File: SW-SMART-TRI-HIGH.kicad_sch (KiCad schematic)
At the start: 53 parts, among them J1 SWLINK, J2 USART1, J3 POWER_OUT, SW0 BTS7002-1EPP, SW1 BTS7002-1EPP, SW2 BTS7002-1EPP, U1 STM32G0B1KBTx, U4 MCP2562-E-SN

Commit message: renamed power in connector
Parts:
- J3: value POWER_OUT -> POWER OUT
- J4: renamed from POWER_IN1; value PWRIN -> POWER IN
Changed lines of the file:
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@@
 		(dnp no)
 		(fields_autoplaced yes)
-		(property "Reference" "POWER_IN1"
+		(property "Reference" "J4"
 			(at 80.01 39.37 0)
 			(effects
@@
 			)
 		)
-		(property "Value" "PWRIN"
+		(property "Value" "POWER IN"
 			(at 80.01 41.91 0)
 			(effects
@@
 					(size 1.27 1.27)
 				)
-				(hide yes)
 			)
 		)
@@
 			(project "SW-DUAL-10A"
 				(path "/08d9f551-d314-4c5c-859f-da02a807087d"
-					(reference "POWER_IN1")
+					(reference "J4")
 					(unit 1)
 				)
@@
 			)
 		)
-		(property "Value" "POWER_OUT"
+		(property "Value" "POWER OUT"
 			(at 149.86 148.5901 0)
 			(effects

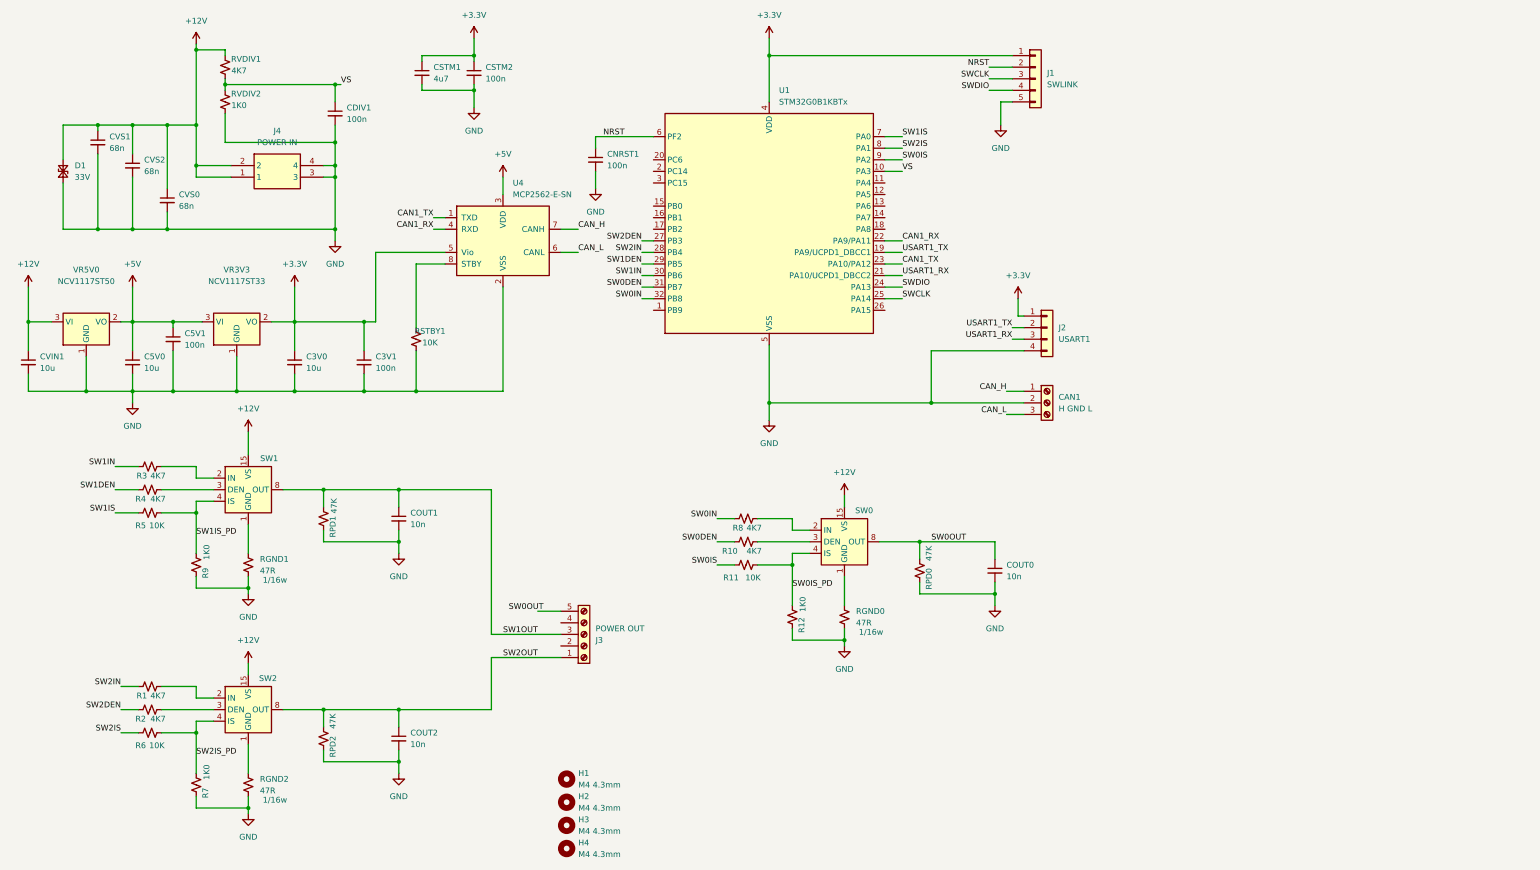
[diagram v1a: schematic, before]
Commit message: switch to smps for 5v, adjust CAN and SWD pin connections
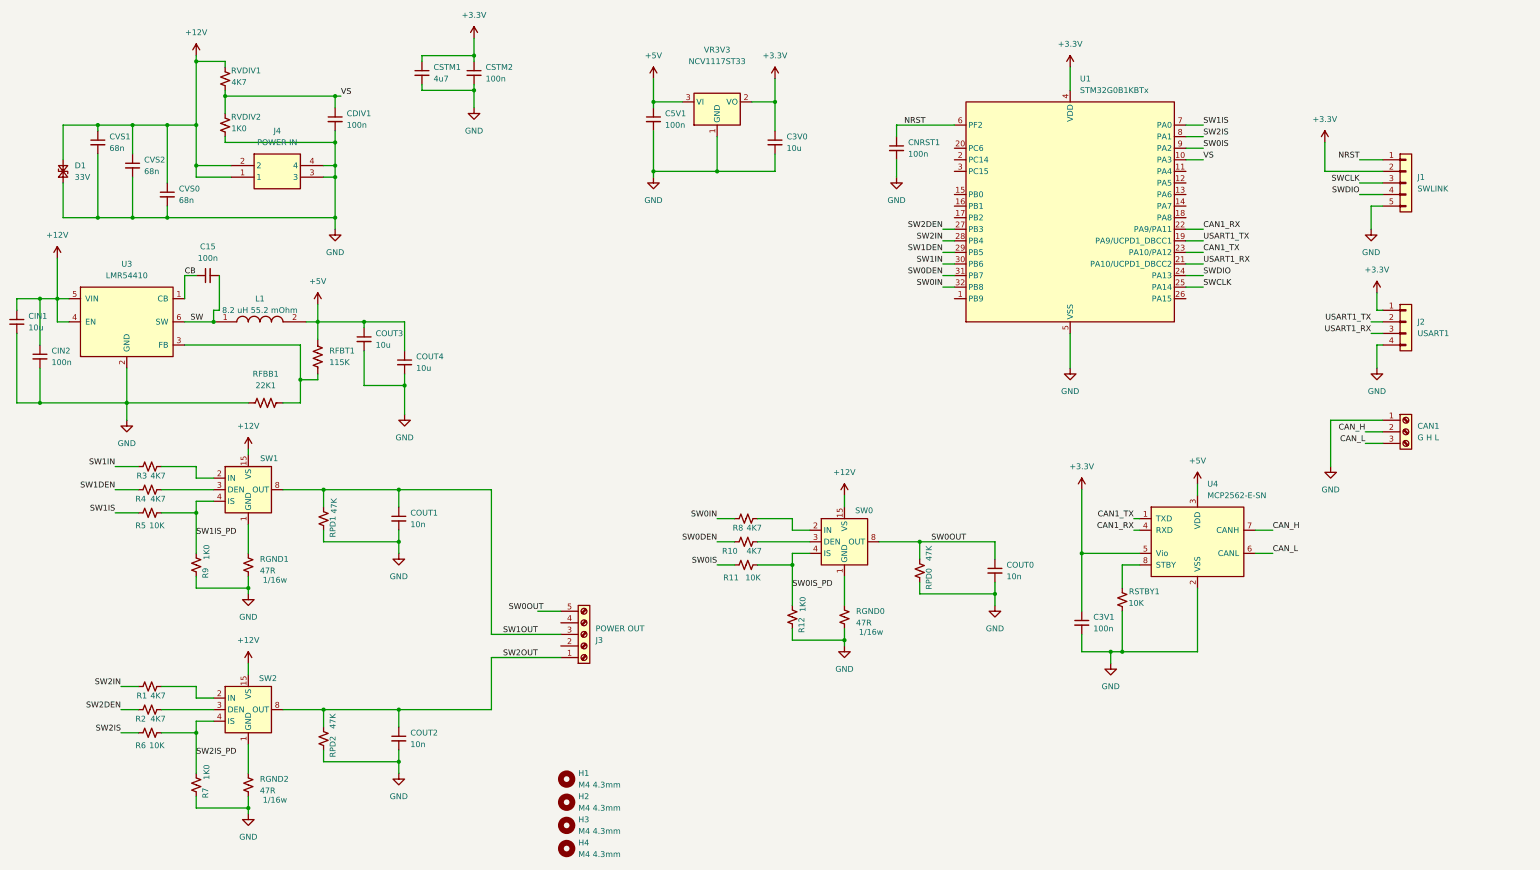
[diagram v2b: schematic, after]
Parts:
- removed C5V0: 10u, Capacitor_SMD:C_0805_2012Metric_Pad1.18x1.45mm_HandSolder, symbol Device:C_Small
- removed CVIN1: 10u, Capacitor_SMD:C_1206_3216Metric_Pad1.33x1.80mm_HandSolder, symbol Device:C_Small
- removed VR5V0: NCV1117ST50, PCM_SparkFun-Semiconductor-Standard:SOT-223-3_TabPin2, symbol PCM_SparkFun-Regulator:LM1117-3.3
- added C15, CIN2: 100n, Capacitor_SMD:C_0603_1608Metric_Pad1.08x0.95mm_HandSolder, symbol Device:C_Small
- added CIN1: 10u, Capacitor_SMD:C_1210_3225Metric_Pad1.33x2.70mm_HandSolder, symbol Device:C_Small
- added COUT3, COUT4: 10u, Capacitor_SMD:C_0805_2012Metric_Pad1.18x1.45mm_HandSolder, symbol Device:C_Small
- added L1: 8.2 uH 55.2 mOhm, SRP5030HMT2R2M, symbol SamacSys_Parts:SRP5030HMT-8R2M
- added RFBB1: 22K1, Resistor_SMD:R_0603_1608Metric_Pad0.98x0.95mm_HandSolder, symbol Device:R_US
- added RFBT1: 115K, Resistor_SMD:R_0603_1608Metric_Pad0.98x0.95mm_HandSolder, symbol Device:R_US
- added U3: LMR54410, Package_TO_SOT_SMD:SOT-23-6, symbol Regulator_Switching:LMR50410
- CAN1: value H GND L -> G H L; footprint TerminalBlock_Phoenix:TerminalBlock_Phoenix_MKDS-1,5-3-5.08_1x03_P5.08mm_Horizontal -> TerminalBlock_Phoenix:TerminalBlock_Phoenix_MPT-0,5-3-2.54_1x03_P2.54mm_Horizontal
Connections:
- net +12V: now also CIN1.1, CIN2.1, U3.4 (EN), U3.5 (VIN)
- net +3.3V: now also J1.2 (Pin_2); no longer J1.1 (Pin_1)
- net +5V: now also COUT3.1, COUT4.1, L1.2, RFBT1.1
- net CAN_H: now also CAN1.2 (Pin_2); no longer CAN1.1 (Pin_1)
- net GND: now also CAN1.1 (Pin_1), CIN1.2, CIN2.2, COUT3.2, COUT4.2, RFBB1.1, U3.2 (GND); no longer CAN1.2 (Pin_2)
- net NRST: now also J1.1 (Pin_1); no longer J1.2 (Pin_2)
- new net: RFBB1.2, RFBT1.2, U3.3 (FB)
- new net CB: C15.1, U3.1 (CB)
- new net SW: C15.2, L1.1, U3.6 (SW)
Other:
- moved on the sheet: C3V0, C3V1, C5V1, CAN1, CDIV1, CNRST1, CVS0, J1, J2, RSTBY1, RVDIV1, RVDIV2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

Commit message: improve ground connections, cleanup silkscreen
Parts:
- SW0: footprint SamacSys_Parts:SOP65P600X115-15N -> Package_SO:Infineon_PG-TSDSO-14-22
- SWD1: renamed from J1; value SWLINK -> RST 3V3 CLK DIO GND; footprint PCM_SparkFun-Connector:1x05_P2.54mm_Locking -> Connector_PinHeader_2.54mm:PinHeader_1x05_P2.54mm_Vertical
- USART1: renamed from J2; value USART1 -> 3V3 TX RX GND; footprint PCM_SparkFun-Connector:1x04_P2.54mm_Locking -> Connector_PinHeader_2.54mm:PinHeader_1x04_P2.54mm_Vertical
- renumbered C15 to CB1
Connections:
- net FB: now reaches RFBB1.2, RFBT1.2, U3.3 (FB)
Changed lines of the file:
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@@
 		)
 	)
+	(label "FB"
+		(at 67.31 86.36 0)
+		(effects
+			(font
+				(size 1.27 1.27)
+			)
+			(justify left bottom)
+		)
+	)
 	(label "SW2DEN"
 		(at 45.72 166.37 180)
@@
 			)
 		)
-		(property "Footprint" "SamacSys_Parts:SOP65P600X115-15N"
+		(property "Footprint" "Package_SO:Infineon_PG-TSDSO-14-22"
 			(at 181.61 135.89 0)
 			(effects
@@
 		(dnp no)
 		(fields_autoplaced yes)
-		(property "Reference" "C15"
+		(property "Reference" "CB1"
 			(at 64.7763 64.77 90)
 			(effects
@@
 			(project "SW-SMART-TRI-HIGH"
 				(path "/08d9f551-d314-4c5c-859f-da02a807087d"
-					(reference "C15")
+					(reference "CB1")
 					(unit 1)
 				)
@@
 		(dnp no)
 		(fields_autoplaced yes)
-		(property "Reference" "J1"
+		(property "Reference" "SWD1"
 			(at 330.2 49.5299 0)
 			(effects
@@
 			)
 		)
-		(property "Value" "SWLINK"
+		(property "Value" "RST 3V3 CLK DIO GND"
 			(at 330.2 52.0699 0)
 			(effects
@@
 			)
 		)
-		(property "Footprint" "PCM_SparkFun-Connector:1x05_P2.54mm_Locking"
+		(property "Footprint" "Connector_PinHeader_2.54mm:PinHeader_1x05_P2.54mm_Vertical"
 			(at 327.66 50.8 0)
 			(effects
@@
 			(project ""
 				(path "/08d9f551-d314-4c5c-859f-da02a807087d"
-					(reference "J1")
+					(reference "SWD1")
 					(unit 1)
 				)
@@
 		(dnp no)
 		(fields_autoplaced yes)
-		(property "Reference" "J2"
+		(property "Reference" "USART1"
 			(at 330.2 81.2799 0)
 			(effects
@@
 			)
 		)
-		(property "Value" "USART1"
+		(property "Value" "3V3 TX RX GND"
 			(at 330.2 83.8199 0)
 			(effects
@@
 			)
 		)
-		(property "Footprint" "PCM_SparkFun-Connector:1x04_P2.54mm_Locking"
+		(property "Footprint" "Connector_PinHeader_2.54mm:PinHeader_1x04_P2.54mm_Vertical"
 			(at 327.66 81.28 0)
 			(effects
@@
 			(project ""
 				(path "/08d9f551-d314-4c5c-859f-da02a807087d"
-					(reference "J2")
+					(reference "USART1")
 					(unit 1)
 				)

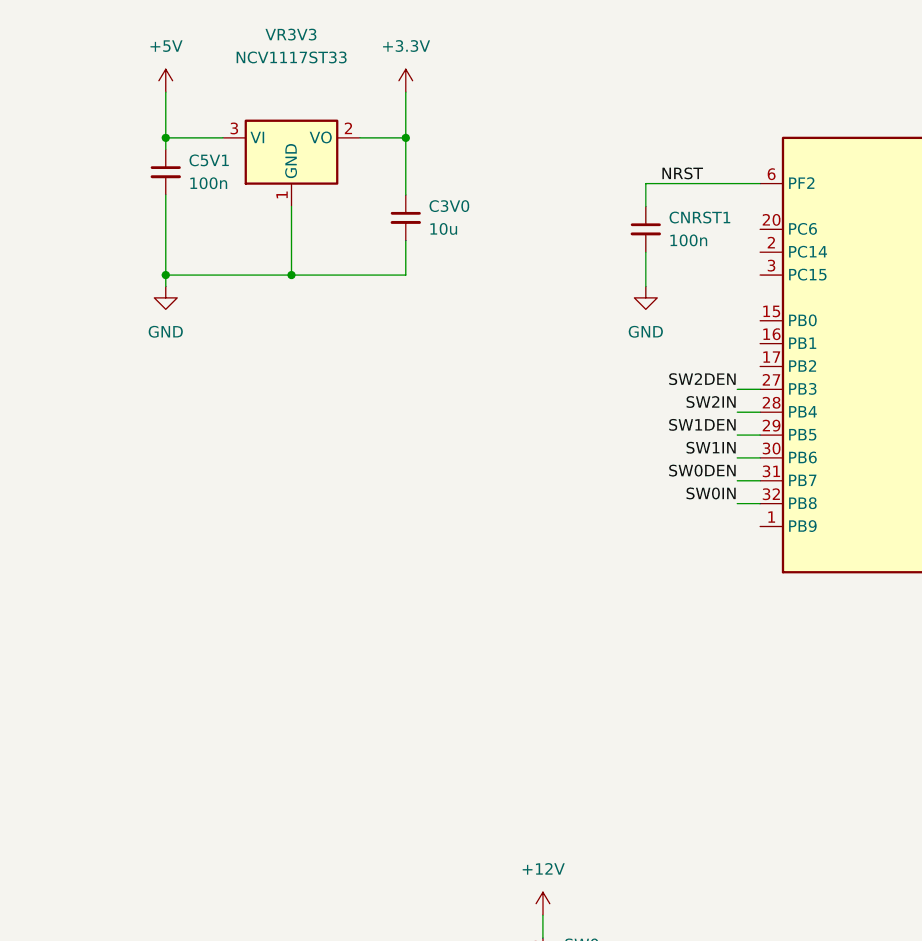
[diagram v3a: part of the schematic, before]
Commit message: add 8mhz XO, fix some footprint issues
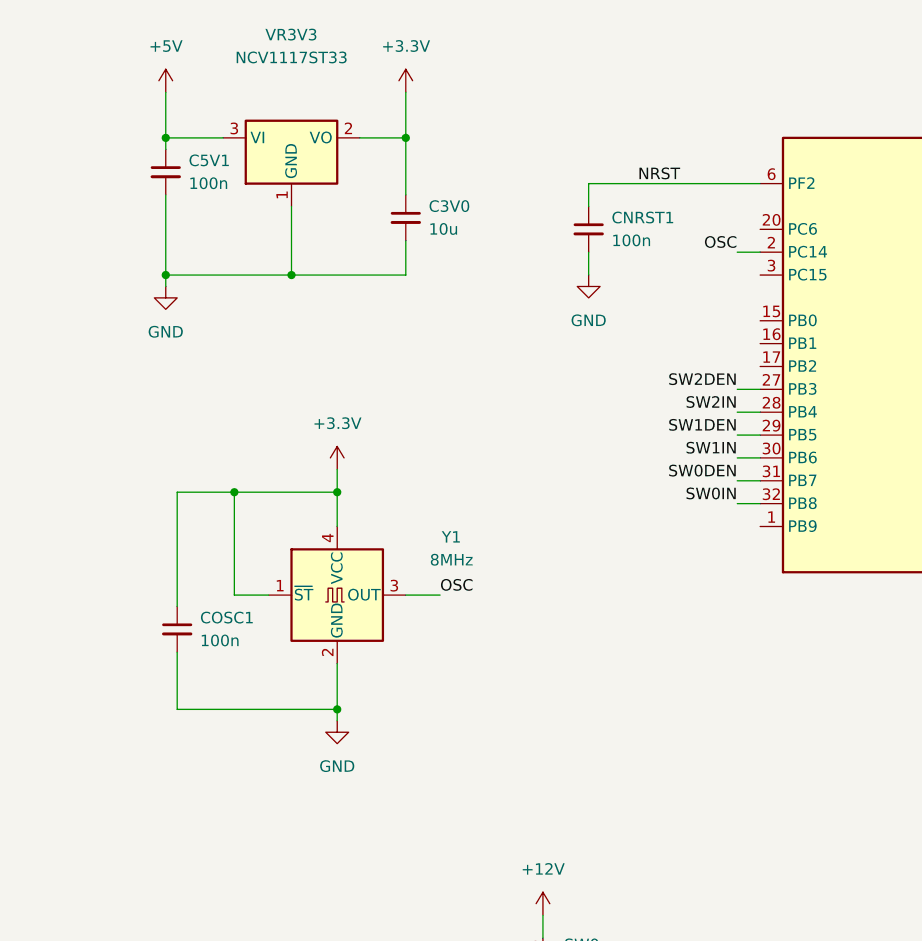
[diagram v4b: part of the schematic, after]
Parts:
- added COSC1: 100n, Capacitor_SMD:C_0603_1608Metric_Pad1.08x0.95mm_HandSolder, symbol Device:C_Small
- added Y1: 8MHz, 3525_4pin_OSC:Oscillator_SMD_XO-4Pin_3.2x2.5mm_HandSoldering, symbol Oscillator:SG-5032CAN
- SW0: footprint Package_SO:Infineon_PG-TSDSO-14-22 -> SamacSys_Parts:SOP65P600X115-15N
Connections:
- net +3.3V: now also COSC1.1, Y1.1 (~{ST}), Y1.4 (VCC)
- net GND: now also COSC1.2, Y1.2 (GND)
- net OSC: now reaches U1.2 (PC14)
- net OSC: now also Y1.3 (OUT)
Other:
- moved on the sheet: CNRST1
